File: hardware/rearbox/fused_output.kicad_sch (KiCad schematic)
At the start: 13 parts, among them U7 VND7020AJTR

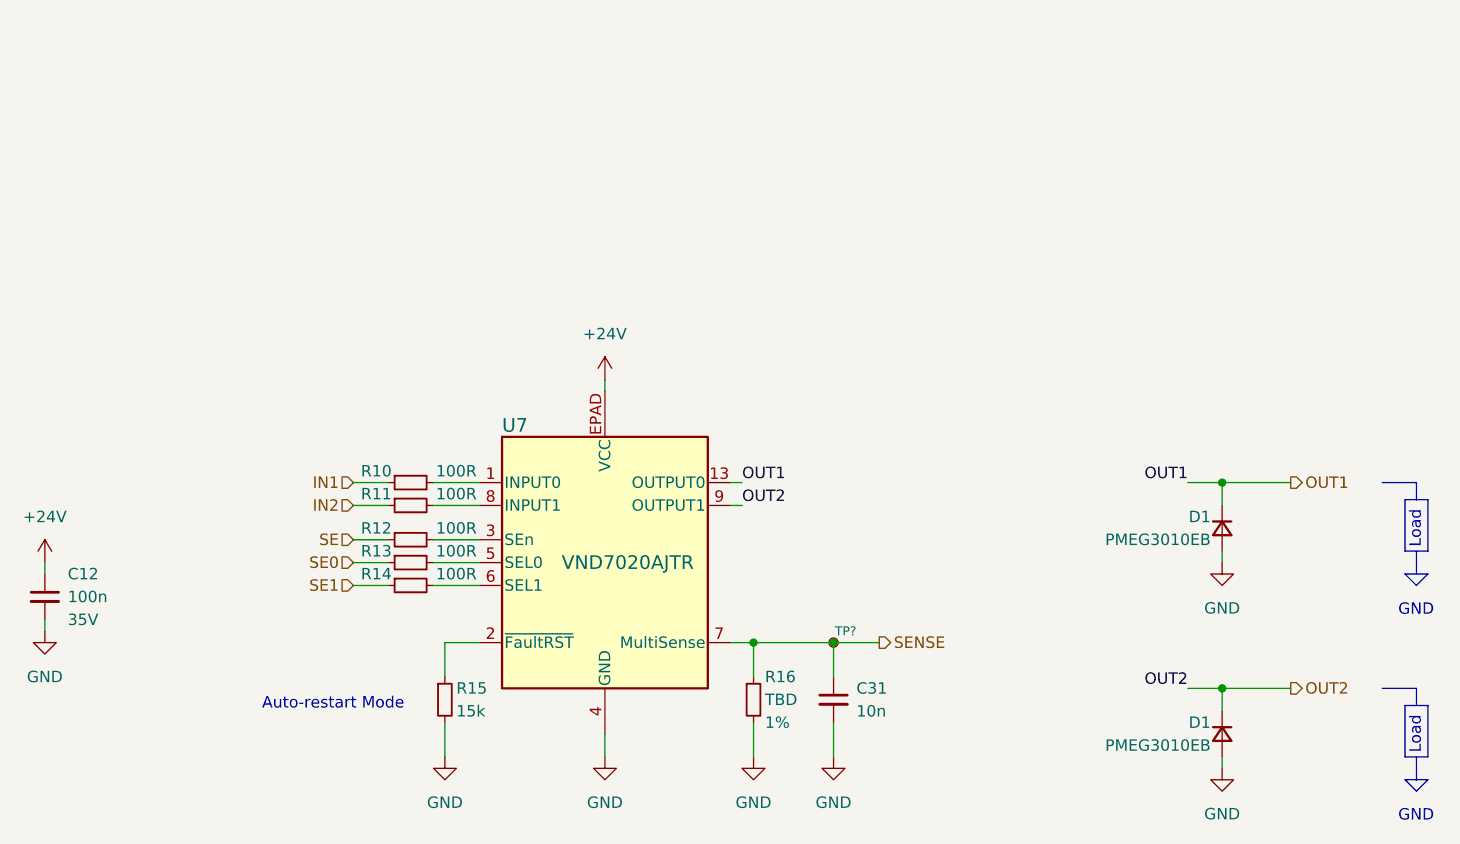
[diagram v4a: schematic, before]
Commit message: Route the tracks on the connector PCB
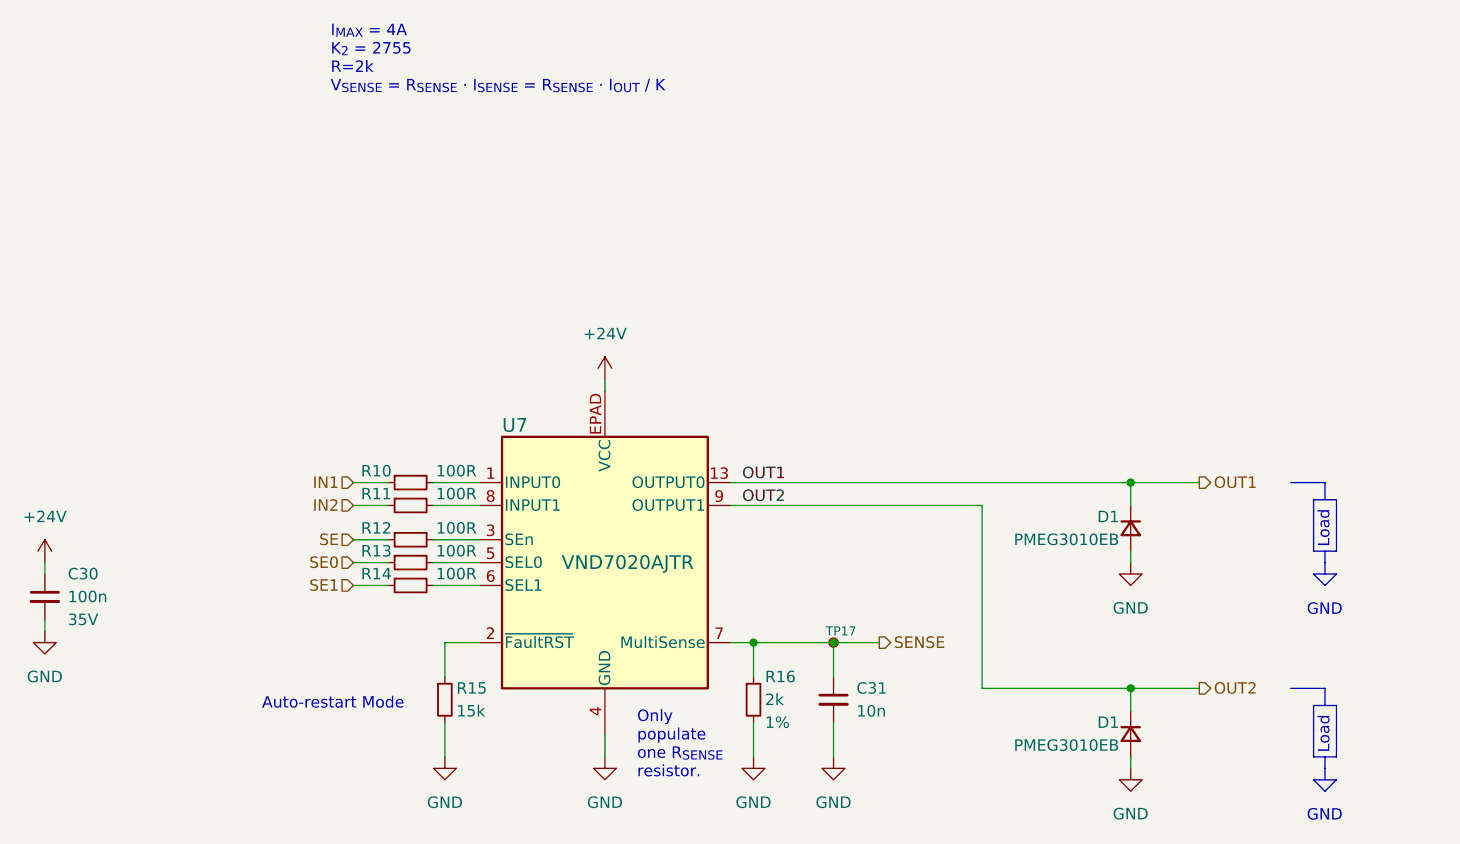
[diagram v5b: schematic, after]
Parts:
- R16: value TBD -> 2k
- gave numbers to parts that had none: 1
- renumbered C12 to C30
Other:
- note added: "I_{MAX} = 4A K_{2} = 2755 R=2k V_{SENSE} = R_{SENSE} · I_{SENSE} = R_{SENSE} · I_{OUT} / K"
- moved on the sheet: D1

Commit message: Fix measurement bridges polarity
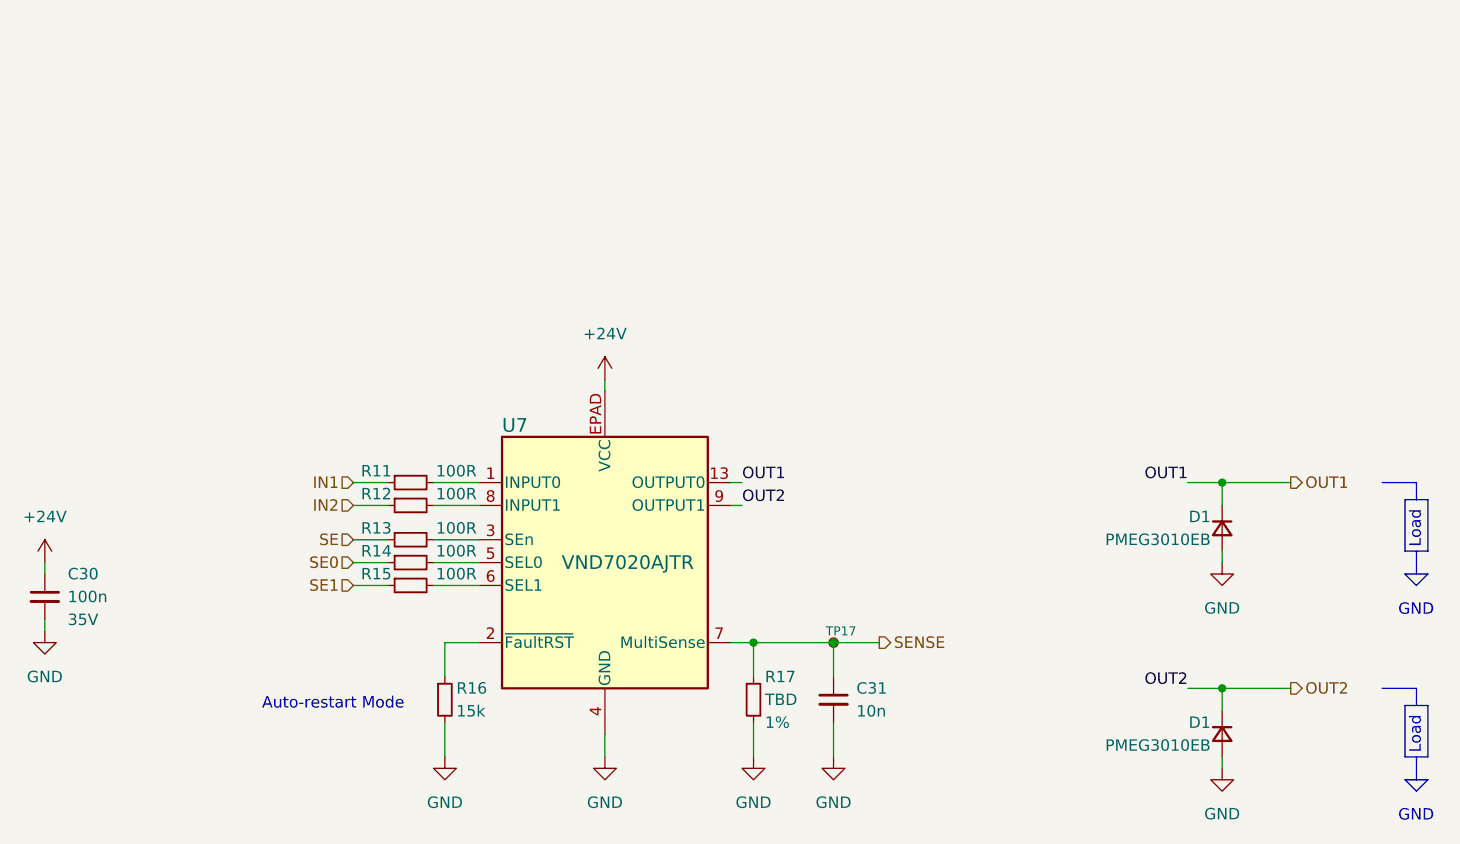
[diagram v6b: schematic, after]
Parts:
- R17: renamed from R16; value 2k -> TBD
- renumbered R10 to R11, R11 to R12, R12 to R13, R13 to R14, R14 to R15, R15 to R16
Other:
- note removed: "I_{MAX} = 4A K_{2} = 2755 R=2k V_{SENSE} = R_{SENSE} · I_{SENSE} = R_{SENSE} · I_{OUT} / K"
- moved on the sheet: D1
